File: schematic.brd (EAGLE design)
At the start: 100 x 70 mm, 9 parts

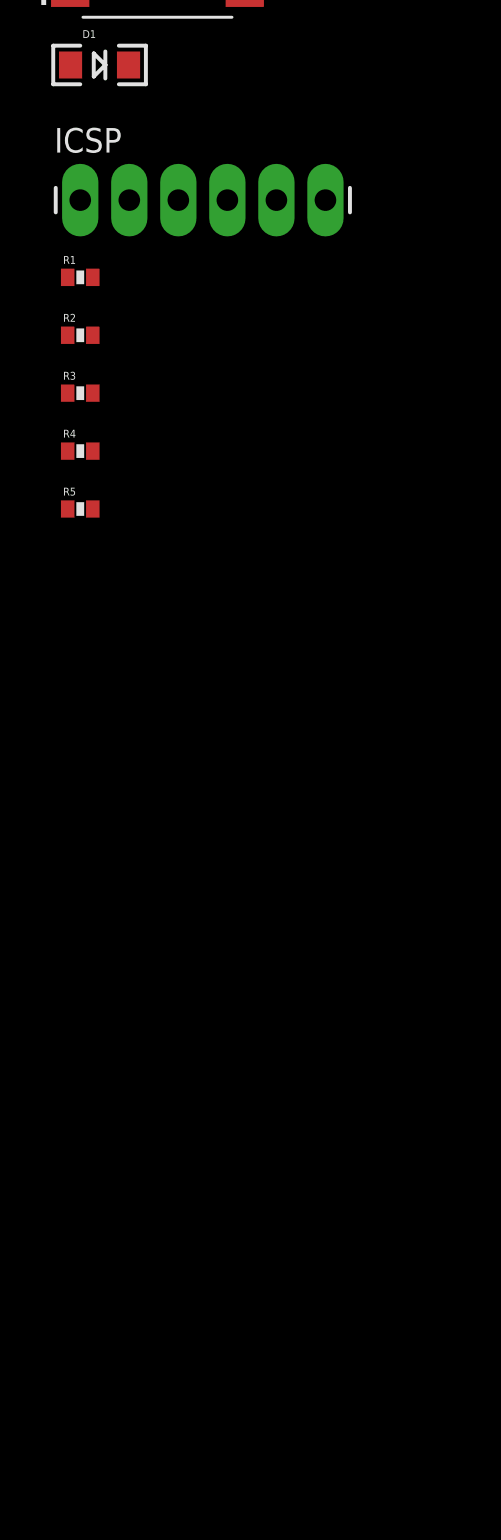
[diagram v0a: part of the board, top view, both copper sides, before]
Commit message: Created schematic for ccentral processor and PWM IO
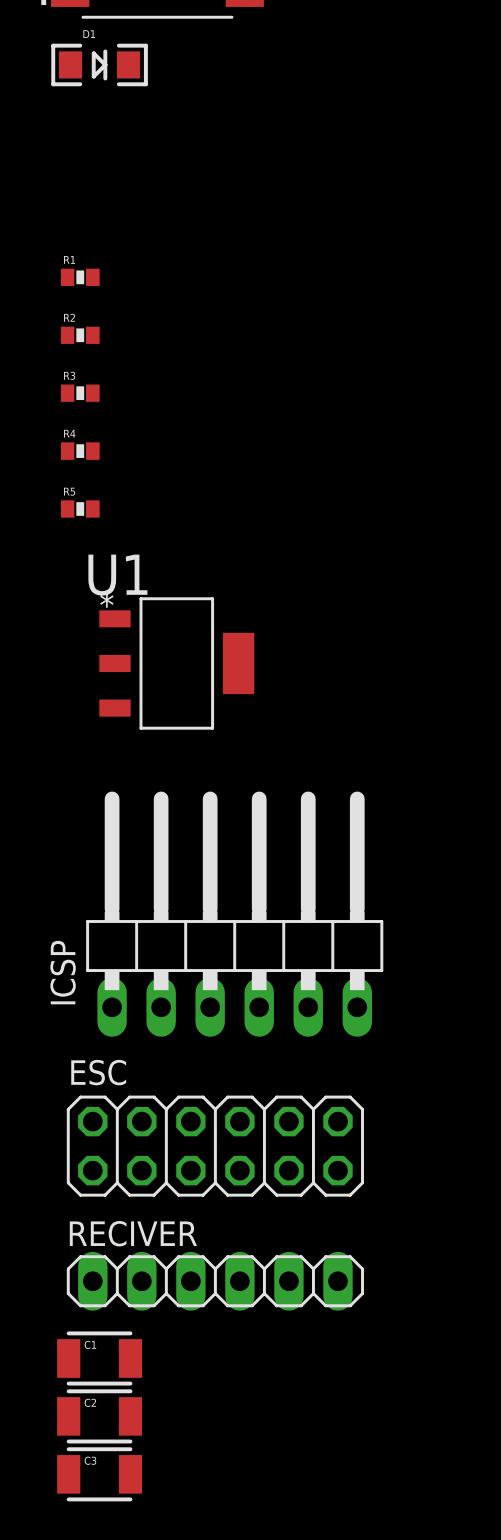
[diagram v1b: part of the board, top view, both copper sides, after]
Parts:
- added C1, C2, C3: 10uF, SparkFun-Capacitors:1210
- added ESC: (no value), pinhead:2X06
- added RECIVER: (no value), pinhead:1X06
- added U1: ADP3338AKCZ-3.3RL7, ADP3338AKCZ-3.3RL7:SOT230P700X180-4N
- ICSP: device SparkFun-Connectors:1X06_LONGPADS -> pinhead:1X06/90
- moved ICSP 38.8 mm to (-49.0, -78.0)
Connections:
- removed net PGC: ICSP.5, MAIN_CONTROLLER.18
- removed net PGD: ICSP.4, MAIN_CONTROLLER.19
- new net 5V: C1.2, ESC.1, U1.3
- new net GND: C1.1, C2.1, C3.2, ESC.3, ICSP.1, MAIN_CONTROLLER.20, R4.2, R5.2, RECIVER.2, U1.1
- new net M1: ESC.5, MAIN_CONTROLLER.5
- new net M2: ESC.7, MAIN_CONTROLLER.6
- new net M3: ESC.9, MAIN_CONTROLLER.7
- new net M4: ESC.11, MAIN_CONTROLLER.14
- new net PGC/ROLL: ICSP.5, MAIN_CONTROLLER.18, RECIVER.4
- new net PGD/PITCH: ICSP.4, MAIN_CONTROLLER.19, RECIVER.3
- new net THROTTLE: MAIN_CONTROLLER.15, RECIVER.6
- new net YAW: MAIN_CONTROLLER.17, RECIVER.5
- net VDD: now also C2.2, C3.1, RECIVER.1, U1.2, U1.4
- net VPP: no longer ICSP.1
- net VSS: no longer MAIN_CONTROLLER.20, R4.2, R5.2
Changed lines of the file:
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@@
 <attribute name="PROD_ID" value="DIO-00862" x="-56" y="-33" size="1.778" layer="27" display="off"/>
 </element>
-<element name="ICSP" library="SparkFun-Connectors" package="1X06_LONGPADS" value="" x="-57" y="-40"/>
 <element name="R1" library="SparkFun-Passives" package="0402-RES" value="10k" x="-57" y="-44"/>
 <element name="R2" library="SparkFun-Passives" package="0402-RES" value="49.9" x="-57" y="-47"/>
@@
 <element name="R4" library="SparkFun-Passives" package="0402-RES" value="49.9" x="-57" y="-53"/>
 <element name="R5" library="SparkFun-Passives" package="0402-RES" value="49.9" x="-57" y="-56"/>
+<element name="U1" library="ADP3338AKCZ-3.3RL7" package="SOT230P700X180-4N" value="ADP3338AKCZ-3.3RL7" x="-52" y="-64"/>
+<element name="ICSP" library="pinhead" package="1X06/90" value="" x="-49" y="-78"/>
+<element name="ESC" library="pinhead" package="2X06" value="" x="-50" y="-89"/>
+<element name="RECIVER" library="pinhead" package="1X06" value="" x="-50" y="-96"/>
+<element name="C1" library="SparkFun-Capacitors" package="1210" value="10uF" x="-56" y="-100">
+<attribute name="PROD_ID" value="CAP-09824" x="-56" y="-100" size="1.778" layer="27" display="off"/>
+</element>
+<element name="C2" library="SparkFun-Capacitors" package="1210" value="10uF" x="-56" y="-103">
+<attribute name="PROD_ID" value="CAP-09824" x="-56" y="-103" size="1.778" layer="27" display="off"/>
+</element>
+<element name="C3" library="SparkFun-Capacitors" package="1210" value="10uF" x="-56" y="-106">
+<attribute name="PROD_ID" value="CAP-09824" x="-56" y="-106" size="1.778" layer="27" display="off"/>
+</element>
 </elements>
 <signals>
@@
 </signal>
 <signal name="VDD">
-<contactref element="ICSP" pad="2"/>
 <contactref element="R1" pad="2"/>
 <contactref element="D1" pad="A"/>
 <contactref element="MAIN_CONTROLLER" pad="1"/>
-<wire x1="-54.46" y1="-40" x2="-56.35" y2="-44" width="0" layer="19" extent="1-1"/>
-<wire x1="-57.5" y1="-33" x2="-54.46" y2="-40" width="0" layer="19" extent="1-1"/>
+<contactref element="U1" pad="4"/>
+<contactref element="U1" pad="2"/>
+<contactref element="ICSP" pad="2"/>
+<contactref element="RECIVER" pad="1"/>
+<contactref element="C2" pad="2"/>
+<contactref element="C3" pad="1"/>
+<wire x1="-54.4" y1="-103" x2="-57.6" y2="-106" width="0" layer="19" extent="1-1"/>
+<wire x1="-56.35" y1="-96" x2="-54.4" y2="-103" width="0" layer="19" extent="1-1"/>
+<wire x1="-52.81" y1="-81.81" x2="-56.35" y2="-96" width="0" layer="19" extent="1-1"/>
+<wire x1="-55.2004" y1="-64" x2="-52.81" y2="-81.81" width="0" layer="19" extent="1-1"/>
+<wire x1="-48.7996" y1="-64" x2="-55.2004" y2="-64" width="0" layer="19" extent="1-1"/>
+<wire x1="-56.35" y1="-44" x2="-55.2004" y2="-64" width="0" layer="19" extent="1-1"/>
+<wire x1="-57.5" y1="-33" x2="-56.35" y2="-44" width="0" layer="19" extent="1-1"/>
 <wire x1="-57.5212" y1="-18.285" x2="-57.5" y2="-33" width="0" layer="19" extent="1-1"/>
 </signal>
 <signal name="VSS">
 <contactref element="ICSP" pad="3"/>
-<contactref element="R4" pad="2"/>
-<contactref element="R5" pad="2"/>
-<contactref element="MAIN_CONTROLLER" pad="20"/>
-<wire x1="-56.35" y1="-53" x2="-56.35" y2="-56" width="0" layer="19" extent="1-1"/>
-<wire x1="-51.92" y1="-40" x2="-56.35" y2="-53" width="0" layer="19" extent="1-1"/>
-<wire x1="-48.4788" y1="-18.285" x2="-51.92" y2="-40" width="0" layer="19" extent="1-1"/>
 </signal>
 <signal name="VPP">
-<contactref element="ICSP" pad="1"/>
 <contactref element="MAIN_CONTROLLER" pad="4"/>
 <contactref element="R1" pad="1"/>
-<wire x1="-57" y1="-40" x2="-57.65" y2="-44" width="0" layer="19" extent="1-1"/>
-<wire x1="-57.5212" y1="-22.095" x2="-57" y2="-40" width="0" layer="19" extent="1-1"/>
-</signal>
-<signal name="PGD">
-<contactref element="ICSP" pad="4"/>
-<contactref element="MAIN_CONTROLLER" pad="19"/>
-<wire x1="-48.4788" y1="-19.555" x2="-49.38" y2="-40" width="0" layer="19" extent="1-1"/>
-</signal>
-<signal name="PGC">
-<contactref element="ICSP" pad="5"/>
-<contactref element="MAIN_CONTROLLER" pad="18"/>
-<wire x1="-48.4788" y1="-20.825" x2="-46.84" y2="-40" width="0" layer="19" extent="1-1"/>
-</signal>
-<signal name="LVP">
-<contactref element="ICSP" pad="6"/>
+<wire x1="-57.5212" y1="-22.095" x2="-57.65" y2="-44" width="0" layer="19" extent="1-1"/>
 </signal>
 <signal name="N$2">
@@
 <wire x1="-54.5" y1="-33" x2="-57.65" y2="-47" width="0" layer="19" extent="1-1"/>
 </signal>
+<signal name="5V">
+<contactref element="U1" pad="3"/>
+<contactref element="ESC" pad="1"/>
+<contactref element="C1" pad="2"/>
+<wire x1="-56.35" y1="-90.27" x2="-54.4" y2="-100" width="0" layer="19" extent="1-1"/>
+<wire x1="-55.2004" y1="-66.3114" x2="-56.35" y2="-90.27" width="0" layer="19" extent="1-1"/>
+</signal>
+<signal name="GND">
+<contactref element="U1" pad="1"/>
+<contactref element="ESC" pad="3"/>
+<contactref element="RECIVER" pad="2"/>
+<contactref element="MAIN_CONTROLLER" pad="20"/>
+<contactref element="R4" pad="2"/>
+<contactref element="R5" pad="2"/>
+<contactref element="ICSP" pad="1"/>
+<contactref element="C3" pad="2"/>
+<contactref element="C1" pad="1"/>
+<contactref element="C2" pad="1"/>
+<wire x1="-57.6" y1="-103" x2="-54.4" y2="-106" width="0" layer="19" extent="1-1"/>
+<wire x1="-57.6" y1="-100" x2="-57.6" y2="-103" width="0" layer="19" extent="1-1"/>
+<wire x1="-53.81" y1="-96" x2="-57.6" y2="-100" width="0" layer="19" extent="1-1"/>
+<wire x1="-53.81" y1="-90.27" x2="-53.81" y2="-96" width="0" layer="19" extent="1-1"/>
+<wire x1="-55.35" y1="-81.81" x2="-53.81" y2="-90.27" width="0" layer="19" extent="1-1"/>
+<wire x1="-55.2004" y1="-61.6886" x2="-55.35" y2="-81.81" width="0" layer="19" extent="1-1"/>
+<wire x1="-56.35" y1="-56" x2="-55.2004" y2="-61.6886" width="0" layer="19" extent="1-1"/>
+<wire x1="-56.35" y1="-53" x2="-56.35" y2="-56" width="0" layer="19" extent="1-1"/>
+<wire x1="-48.4788" y1="-18.285" x2="-56.35" y2="-53" width="0" layer="19" extent="1-1"/>
+</signal>
+<signal name="LVP">
+<contactref element="ICSP" pad="6"/>
+</signal>
+<signal name="M1">
+<contactref element="ESC" pad="5"/>
+<contactref element="MAIN_CONTROLLER" pad="5"/>
+<wire x1="-57.5212" y1="-23.365" x2="-51.27" y2="-90.27" width="0" layer="19" extent="1-1"/>
+</signal>
+<signal name="M2">
+<contactref element="ESC" pad="7"/>
+<contactref element="MAIN_CONTROLLER" pad="6"/>
+<wire x1="-57.5212" y1="-24.635" x2="-48.73" y2="-90.27" width="0" layer="19" extent="1-1"/>
+</signal>
+<signal name="M3">
+<contactref element="ESC" pad="9"/>
+<contactref element="MAIN_CONTROLLER" pad="7"/>
+<wire x1="-57.5212" y1="-25.905" x2="-46.19" y2="-90.27" width="0" layer="19" extent="1-1"/>
+</signal>
+<signal name="M4">
+<contactref element="ESC" pad="11"/>
+<contactref element="MAIN_CONTROLLER" pad="14"/>
+<wire x1="-48.4788" y1="-25.905" x2="-43.65" y2="-90.27" width="0" layer="19" extent="1-1"/>
+</signal>
+<signal name="YAW">
+<contactref element="RECIVER" pad="5"/>
+<contactref element="MAIN_CONTROLLER" pad="17"/>
+<wire x1="-48.4788" y1="-22.095" x2="-46.19" y2="-96" width="0" layer="19" extent="1-1"/>
+</signal>
+<signal name="THROTTLE">
+<contactref element="RECIVER" pad="6"/>
+<contactref element="MAIN_CONTROLLER" pad="15"/>
+<wire x1="-48.4788" y1="-24.635" x2="-43.65" y2="-96" width="0" layer="19" extent="1-1"/>
+</signal>
+<signal name="PGD/PITCH">
+<contactref element="ICSP" pad="4"/>
+<contactref element="RECIVER" pad="3"/>
+<contactref element="MAIN_CONTROLLER" pad="19"/>
+<wire x1="-47.73" y1="-81.81" x2="-51.27" y2="-96" width="0" layer="19" extent="1-1"/>
+<wire x1="-48.4788" y1="-19.555" x2="-47.73" y2="-81.81" width="0" layer="19" extent="1-1"/>
+</signal>
+<signal name="PGC/ROLL">
+<contactref element="ICSP" pad="5"/>
+<contactref element="RECIVER" pad="4"/>
+<contactref element="MAIN_CONTROLLER" pad="18"/>
+<wire x1="-45.19" y1="-81.81" x2="-48.73" y2="-96" width="0" layer="19" extent="1-1"/>
+<wire x1="-48.4788" y1="-20.825" x2="-45.19" y2="-81.81" width="0" layer="19" extent="1-1"/>
+</signal>
 </signals>

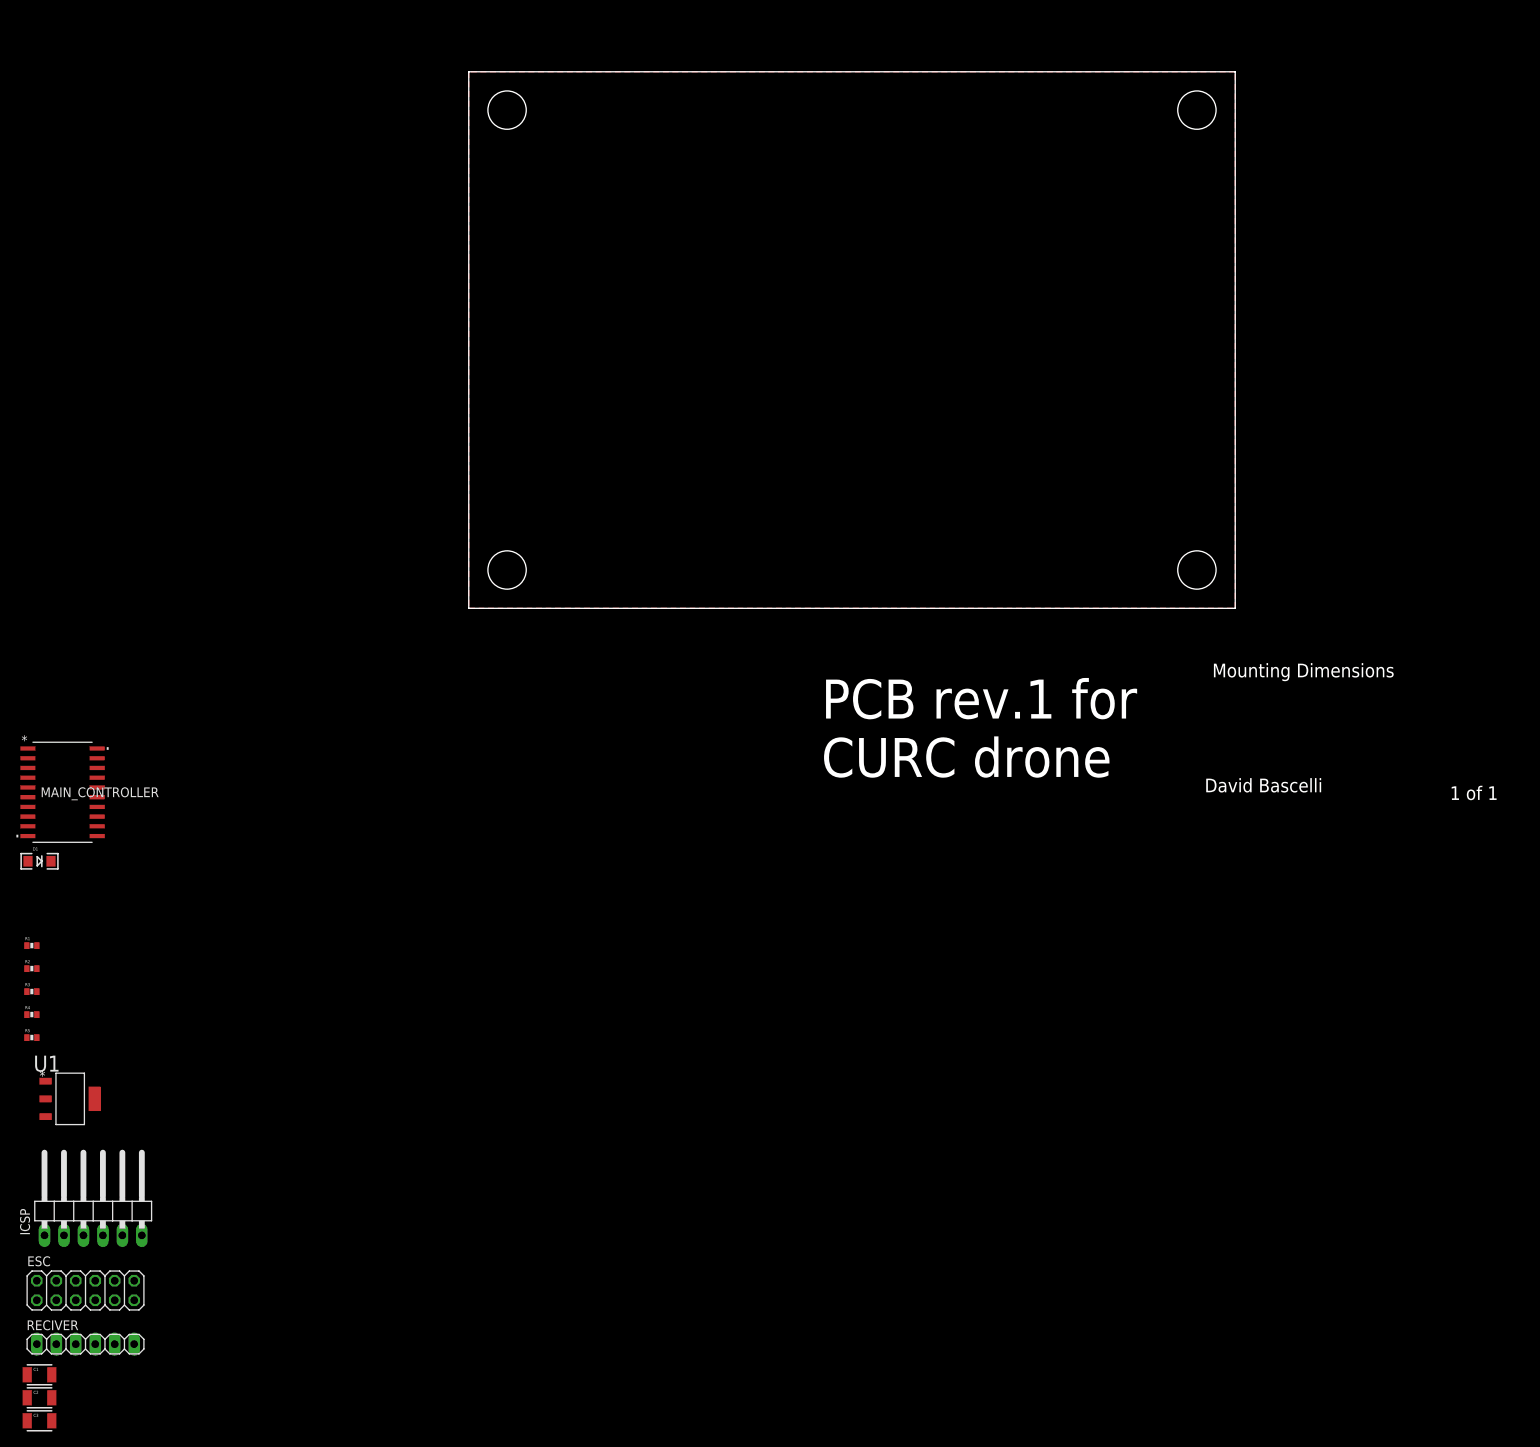
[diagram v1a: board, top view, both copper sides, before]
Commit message: Attached IMU and XBEE in schematic. Schematic is now done unless the extra outputs from the xbee are needed
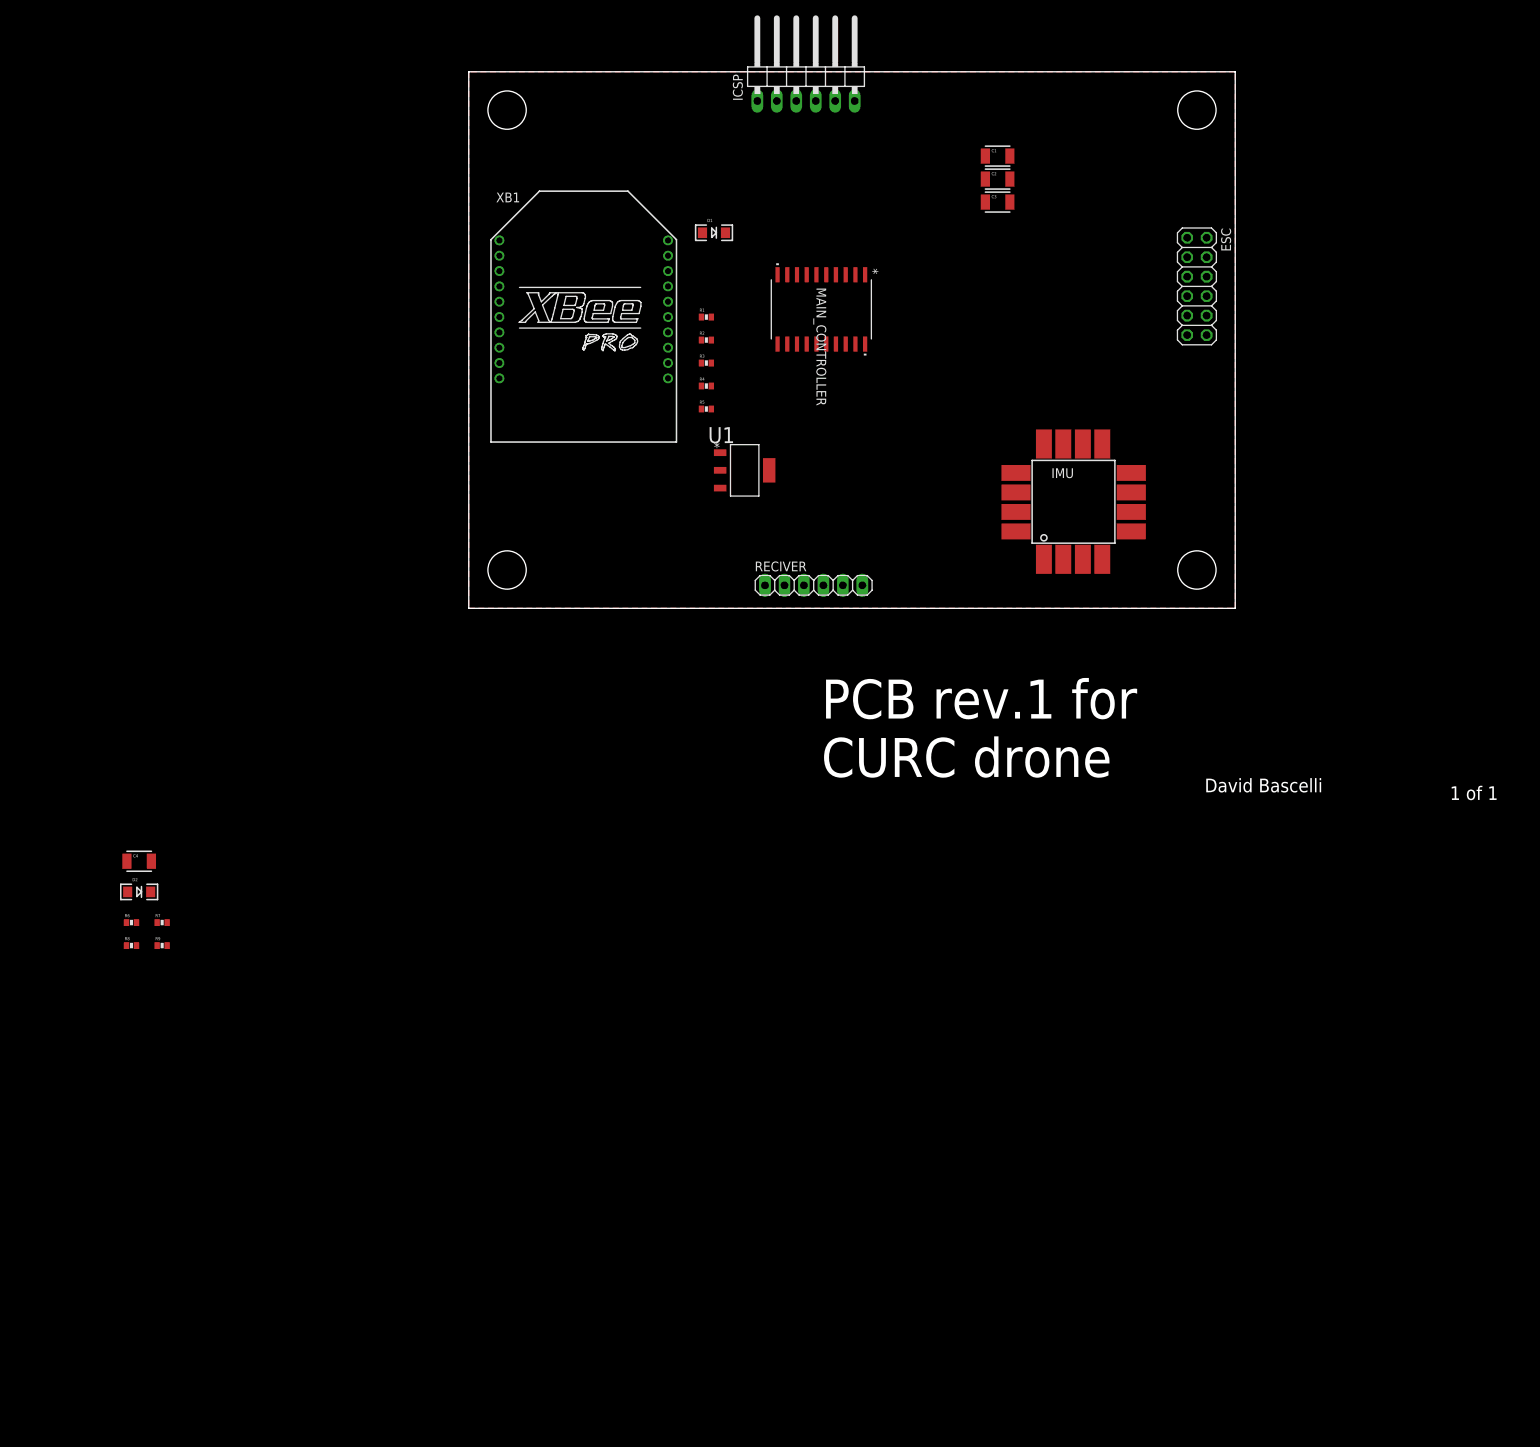
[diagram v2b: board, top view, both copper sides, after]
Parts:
- added C4: 10uF, SparkFun-Capacitors:1210
- added D2: GREEN, SparkFun-LED:LED-1206
- added IMU: MM7150, MM7150:LANDPATTERN
- added R6, R7, R8, R9: 49.9, SparkFun-Passives:0402-RES
- added XB1: XBEE-PRO, xbee:XBEE-PRO
- moved C1 202.3 mm to (69.0, 59.0)
- moved C2 202.3 mm to (69.0, 56.0)
- moved C3 202.3 mm to (69.0, 53.0)
- moved ESC 195.4 mm to (95.0, 42.0), turned to 270 degrees
- moved ICSP 174.8 mm to (44.0, 70.0)
- moved RECIVER 137.2 mm to (45.0, 3.00)
- moved D1 120.3 mm to (32.0, 49.0)
- moved R1 120.3 mm to (31.0, 38.0)
- moved R2 120.3 mm to (31.0, 35.0)
- moved R3 120.3 mm to (31.0, 32.0)
- moved R4 120.3 mm to (31.0, 29.0)
- moved R5 120.3 mm to (31.0, 26.0)
- moved U1 120.3 mm to (36.0, 18.0)
- moved MAIN_CONTROLLER 117.3 mm to (46.0, 39.0), turned to 270 degrees
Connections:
- new net IMU_INT: IMU.P$4, MAIN_CONTROLLER.9
- new net N$5: C4.1, XB1.5
- new net N$6: R7.2, R9.1
- new net N$7: R6.2, R8.1
- new net N$8: D2.C, R6.1, R7.1
- new net N$9: D2.A, XB1.13
- new net RX: MAIN_CONTROLLER.12, XB1.2
- new net SCL: IMU.P$15, MAIN_CONTROLLER.11
- new net SDA: IMU.P$16, MAIN_CONTROLLER.13
- new net TX: MAIN_CONTROLLER.10, XB1.3
- new net VCC: C4.2, XB1.1
- net GND: now also IMU.P$8, R8.2, R9.2, XB1.10
- net VDD: now also IMU.P$7
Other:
- board text removed: "Mounting Dimensions"
